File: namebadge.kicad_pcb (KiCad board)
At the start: 2 copper layers, 73.7 x 132.1 mm, 30 parts, among them U1 Pico

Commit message: power cap
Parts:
- added C15: 1000uF, Capacitor_THT:C_Radial_D12.5mm_H20.0mm_P5.00mm, F.Cu at (87.1, 47.2)
- moved U1 7.61 mm to (50.0, 33.0)
- moved R1 3.70 mm to (41.1, 53.3)
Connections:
- net Neo_DIN renamed /letter-k/LED_DIN
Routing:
- net VCC: track 392.6 -> 399.6 mm
- net /letter-k/LED_DIN: track 17.3 -> 14.7 mm
- net Net-(R1-Pad2): track 10.5 -> 11.4 mm

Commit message: level shifter
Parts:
- added IC1: SN74AHCT125N, Package_DIP:DIP-14_W7.62mm, F.Cu at (25.7, 55.6)
- moved R1 17.4 mm to (48.0, 69.3), turned to 90 degrees
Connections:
- R1 pad 2: Net-(R1-Pad2) -> Net-(IC1-Pad11)
- U1 pad 21: Net-(R1-Pad2) -> Net-(IC1-Pad12)
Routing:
- net VCC: track 399.6 -> 429.8 mm
- net Net-(IC1-Pad11): track 0.00 -> 18.4 mm
- net Net-(R1-Pad2): track 11.4 -> 0.00 mm
- net Net-(IC1-Pad12): track 0.00 -> 9.58 mm
- net /letter-k/LED_DIN: track 14.7 -> 24.3 mm

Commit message: DC jack take 1
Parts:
- added J1: Barrel_Jack, Connector_BarrelJack:BarrelJack_CUI_PJ-063AH_Horizontal, F.Cu at (80.3, 32.8)
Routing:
- net VCC: track 429.8 -> 441.9 mm
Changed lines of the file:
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@@
     (thickness 1.6)
     (drawings 6)
-    (tracks 133)
+    (tracks 137)
     (zones 0)
-    (modules 32)
+    (modules 33)
     (nets 62)
   )
@@
     )
   )
+  (module Connector_BarrelJack:BarrelJack_CUI_PJ-063AH_Horizontal (layer F.Cu)
+    (at 80.264 32.766 90)
+    (descr "Barrel Jack, 2.0mm ID, 5.5mm OD, 24V, 8A, no switch, https://www.cui.com/product/resource/pj-063ah.pdf")
+    (tags "barrel jack cui dc power")
+    (fp_text reference J1 (at 0 -2.3 90) (layer F.SilkS)
+      (effects (font (size 1 1) (thickness 0.15)))
+    )
+    (fp_text value Barrel_Jack (at 0 13 90) (layer F.Fab)
+      (effects (font (size 1 1) (thickness 0.15)))
+    )
+    (fp_text user %R (at 0 5.5 90) (layer F.Fab)
+      (effects (font (size 1 1) (thickness 0.15)))
+    )
+    (fp_line (start -5 -1) (end -1 -1) (layer F.Fab) (width 0.1))
+    (fp_line (start -1 -1) (end 0 0) (layer F.Fab) (width 0.1))
+    (fp_line (start 0 0) (end 1 -1) (layer F.Fab) (width 0.1))
+    (fp_line (start 1 -1) (end 5 -1) (layer F.Fab) (width 0.1))
+    (fp_line (start 5 -1) (end 5 12) (layer F.Fab) (width 0.1))
+    (fp_line (start 5 12) (end -5 12) (layer F.Fab) (width 0.1))
+    (fp_line (start -5 12) (end -5 -1) (layer F.Fab) (width 0.1))
+    (fp_line (start -5.11 4.95) (end -5.11 -1.11) (layer F.SilkS) (width 0.12))
+    (fp_line (start -5.11 -1.11) (end -2.3 -1.11) (layer F.SilkS) (width 0.12))
+    (fp_line (start 2.3 -1.11) (end 5.11 -1.11) (layer F.SilkS) (width 0.12))
+    (fp_line (start 5.11 -1.11) (end 5.11 4.95) (layer F.SilkS) (width 0.12))
+    (fp_line (start 5.11 9.05) (end 5.11 12.11) (layer F.SilkS) (width 0.12))
+    (fp_line (start 5.11 12.11) (end -5.11 12.11) (layer F.SilkS) (width 0.12))
+    (fp_line (start -5.11 12.11) (end -5.11 9.05) (layer F.SilkS) (width 0.12))
+    (fp_line (start -1 -1.3) (end 1 -1.3) (layer F.SilkS) (width 0.12))
+    (fp_line (start -6 -1.5) (end -6 12.5) (layer F.CrtYd) (width 0.05))
+    (fp_line (start -6 12.5) (end 6 12.5) (layer F.CrtYd) (width 0.05))
+    (fp_line (start 6 12.5) (end 6 -1.5) (layer F.CrtYd) (width 0.05))
+    (fp_line (start 6 -1.5) (end -6 -1.5) (layer F.CrtYd) (width 0.05))
+    (pad "" np_thru_hole circle (at 0 9 90) (size 1.6 1.6) (drill 1.6) (layers *.Cu *.Mask))
+    (pad MP thru_hole oval (at 4.5 7 90) (size 2 3.5) (drill oval 1 2.5) (layers *.Cu *.Mask))
+    (pad MP thru_hole oval (at -4.5 7 90) (size 2 3.5) (drill oval 1 2.5) (layers *.Cu *.Mask))
+    (pad 2 thru_hole oval (at 0 6 90) (size 3.3 2) (drill oval 2.3 1) (layers *.Cu *.Mask)
+      (net 1 GND))
+    (pad 1 thru_hole rect (at 0 0 90) (size 4 2) (drill oval 3 1) (layers *.Cu *.Mask)
+      (net 2 VCC))
+    (model ${KISYS3DMOD}/Connector_BarrelJack.3dshapes/BarrelJack_CUI_PJ-063AH_Horizontal.wrl
+      (at (xyz 0 0 0))
+      (scale (xyz 1 1 1))
+      (rotate (xyz 0 0 0))
+    )
+  )
   (gr_text "\"K\" Namebadge v0.1    @sveiss 2021" (at 78.232 147.828) (layer F.SilkS)
     (effects (font (size 1 1) (thickness 0.15)))
@@
   (segment (start 83.82 54.102) (end 83.82 55.88) (width 0.508) (layer B.Cu) (net 2))
   (segment (start 58.42 54.102) (end 50.8 61.722) (width 0.508) (layer B.Cu) (net 2))
-  (segment (start 74.168 41.91) (end 79.502 47.244) (width 0.508) (layer B.Cu) (net 2))
-  (segment (start 79.502 47.244) (end 82.122 47.244) (width 0.508) (layer B.Cu) (net 2))
   (segment (start 82.122 54.022) (end 82.042 54.102) (width 0.508) (layer B.Cu) (net 2))
   (segment (start 82.122 47.244) (end 82.122 54.022) (width 0.508) (layer B.Cu) (net 2))
@@
   (segment (start 44.196 61.722) (end 37.592 61.722) (width 0.508) (layer B.Cu) (net 2))
   (segment (start 50.8 61.722) (end 44.196 61.722) (width 0.508) (layer B.Cu) (net 2))
+  (segment (start 80.264 32.766) (end 80.264 35.814) (width 0.508) (layer B.Cu) (net 2))
+  (segment (start 80.264 46.99) (end 80.518 47.244) (width 0.508) (layer B.Cu) (net 2))
+  (segment (start 80.518 47.244) (end 82.122 47.244) (width 0.508) (layer B.Cu) (net 2))
+  (segment (start 74.168 41.91) (end 80.264 41.91) (width 0.508) (layer B.Cu) (net 2))
+  (segment (start 80.264 41.91) (end 80.264 46.99) (width 0.508) (layer B.Cu) (net 2))
+  (segment (start 80.264 35.814) (end 80.264 41.91) (width 0.508) (layer B.Cu) (net 2))
   (segment (start 30.48 66.04) (end 30.48 72.263) (width 0.25) (layer F.Cu) (net 36))
   (segment (start 30.48 78.74) (end 30.48 84.963) (width 0.25) (layer F.Cu) (net 37))

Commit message: flip the pico
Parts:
- turned U1 to 90 degrees
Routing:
- net Net-(IC1-Pad12): track 9.58 -> 71.6 mm
- net VCC: track 441.9 -> 501.4 mm
- net Net-(U1-Pad1): track 0.00 -> 3.05 mm

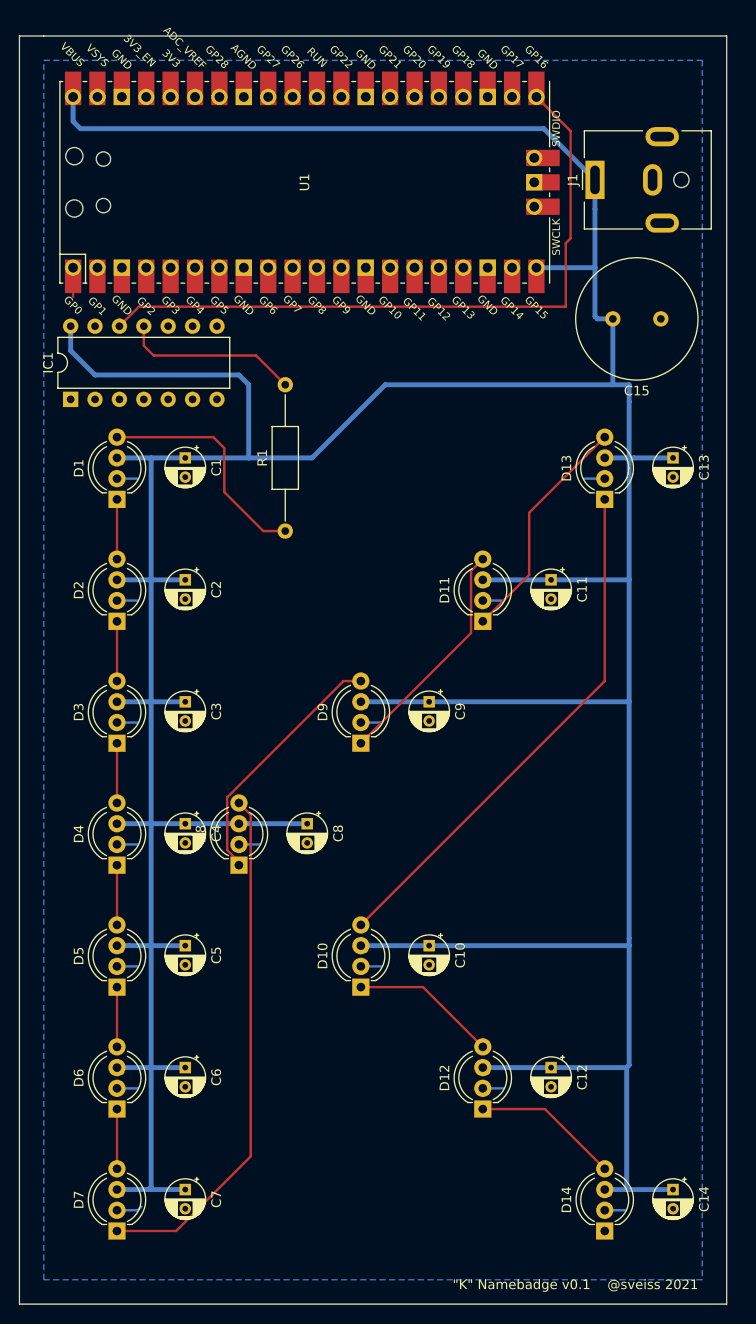
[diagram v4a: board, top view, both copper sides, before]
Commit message: decoup for level shifter, layout cleanup
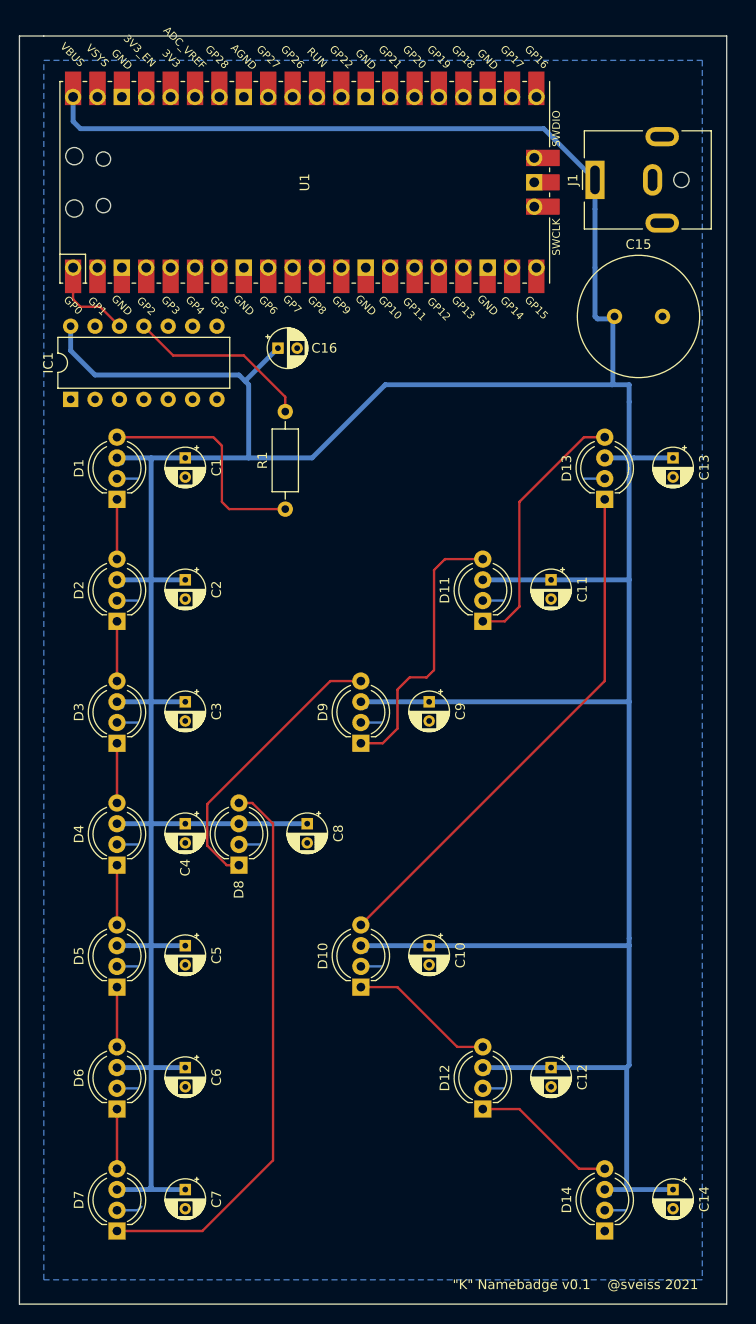
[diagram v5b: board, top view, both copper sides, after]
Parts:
- added C16: 0.1uF, Capacitor_THT:CP_Radial_D4.0mm_P2.00mm, F.Cu at (47.2, 50.3)
- R1: footprint Resistor_THT:R_Axial_DIN0207_L6.3mm_D2.5mm_P15.24mm_Horizontal -> Resistor_THT:R_Axial_DIN0207_L6.3mm_D2.5mm_P10.16mm_Horizontal
- moved C15 4.83 mm to (82.3, 47.0), turned to 0 degrees
- moved R1 2.29 mm to (48.0, 67.1)
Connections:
- C15 pad 1: GND -> VCC
- C15 pad 2: VCC -> GND
- U1 pad 1: Net-(U1-Pad1) -> Net-(IC1-Pad12)
- U1 pad 21: Net-(IC1-Pad12) -> Net-(U1-Pad21)
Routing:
- net Net-(IC1-Pad12): track 71.6 -> 11.6 mm
- net Net-(D11-Pad4): track 24.4 -> 29.1 mm
- net Net-(D7-Pad1): track 54.5 -> 58.8 mm
- net Net-(U1-Pad1): track 3.05 -> 0.00 mm
- net Net-(D8-Pad1): track 27.0 -> 29.8 mm
- net Net-(D11-Pad1): track 24.4 -> 27.0 mm
- net VCC: track 501.4 -> 500.1 mm
- net Net-(IC1-Pad11): track 18.4 -> 19.3 mm

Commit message: switch
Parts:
- added SW1: SW_Push, Button_Switch_THT:SW_PUSH-12mm, F.Cu at (57.1, 52.8)
- C15: footprint Capacitor_THT:C_Radial_D12.5mm_H20.0mm_P5.00mm -> Capacitor_THT:CP_Radial_D12.5mm_P5.00mm
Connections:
- IC1 pad 12: Net-(IC1-Pad12) -> GND
- U1 pad 1: Net-(IC1-Pad12) -> GND
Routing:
- net Net-(SW1-Pad2): track 0.00 -> 31.4 mm
- net Net-(IC1-Pad12): track 11.6 -> 0.00 mm
- net GND: track 30.8 -> 42.4 mm
- net VCC: track 500.1 -> 505.1 mm

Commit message: fix dropped connection to gpio
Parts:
- moved C16 19.8 mm to (27.4, 50.8), turned to 270 degrees
- moved IC1 9.14 mm to (34.8, 55.6)
- moved R1 5.49 mm to (43.4, 70.1), turned to 0 degrees
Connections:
- IC1 pad 12: GND -> Net-(IC1-Pad12)
- U1 pad 1: GND -> Net-(IC1-Pad12)
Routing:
- net Net-(IC1-Pad12): track 0.00 -> 18.9 mm
- net Net-(IC1-Pad11): track 19.3 -> 31.7 mm
- net VCC: track 505.1 -> 493.2 mm
- net GND: track 42.4 -> 30.8 mm
